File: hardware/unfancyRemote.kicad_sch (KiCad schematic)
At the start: 42 parts, among them J3 HALL1/PPM, J4 HALL2, J6 VIN, J7 VBAT, J8 Motor, Q1 AO3401A, Q2 MMBT3904, Q3 MMBT3904, SW1 SW_Push, U1 E28-2G4M12S, U2 MCP73871-2AA, U3 ESP32-C3_SUPERMINI

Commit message: wip
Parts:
- U3: footprint ESP32-C3_SUPERMINI:MODULE_ESP32-C3_SUPERMINI -> unfancyRemote_components:MODULE_ESP32-C3_SUPERMINI; symbol ESP32-C3_SUPERMINI:ESP32-C3_SUPERMINI -> unfancyRemote_components:ESP32-C3_SUPERMINI
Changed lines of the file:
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@@
 	)
 	(symbol
-		(lib_id "ESP32-C3_SUPERMINI:ESP32-C3_SUPERMINI")
+		(lib_id "unfancyRemote_components:ESP32-C3_SUPERMINI")
 		(at 135.89 36.83 0)
 		(unit 1)
@@
 			)
 		)
-		(property "Footprint" "ESP32-C3_SUPERMINI:MODULE_ESP32-C3_SUPERMINI"
+		(property "Footprint" "unfancyRemote_components:MODULE_ESP32-C3_SUPERMINI"
 			(at 135.89 36.83 0)
 			(effects

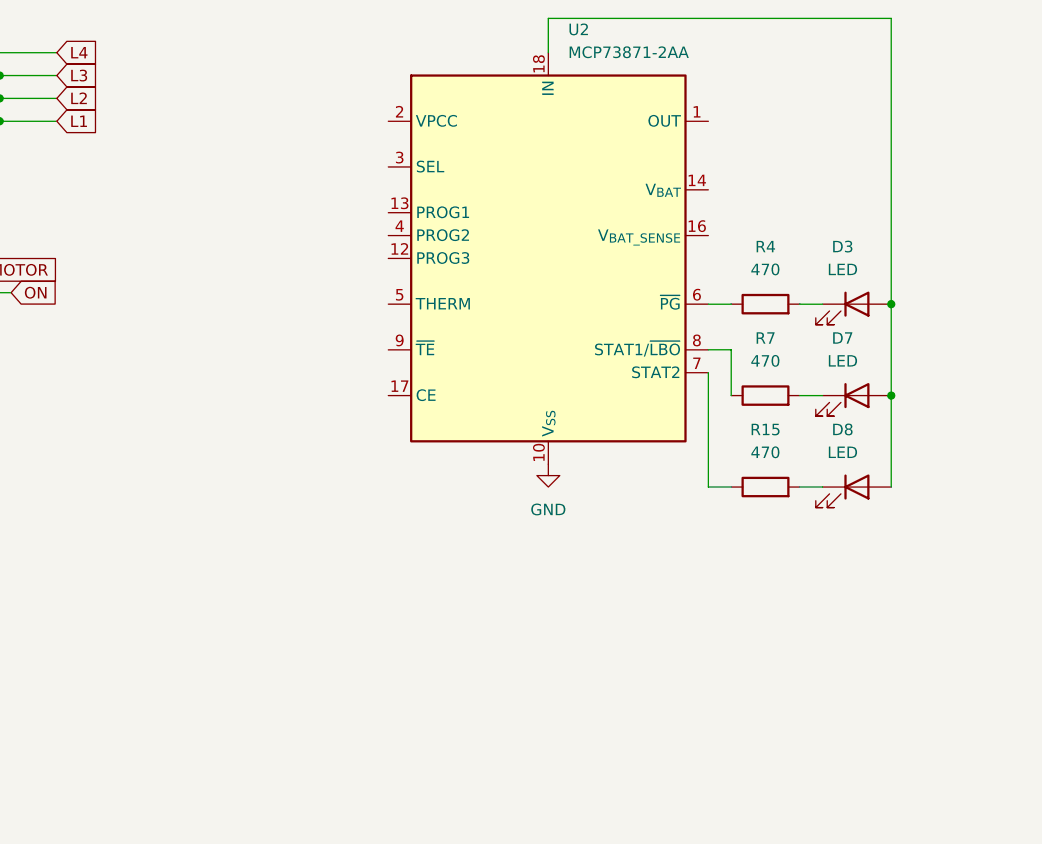
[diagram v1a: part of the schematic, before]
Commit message: finished charging ic wiring
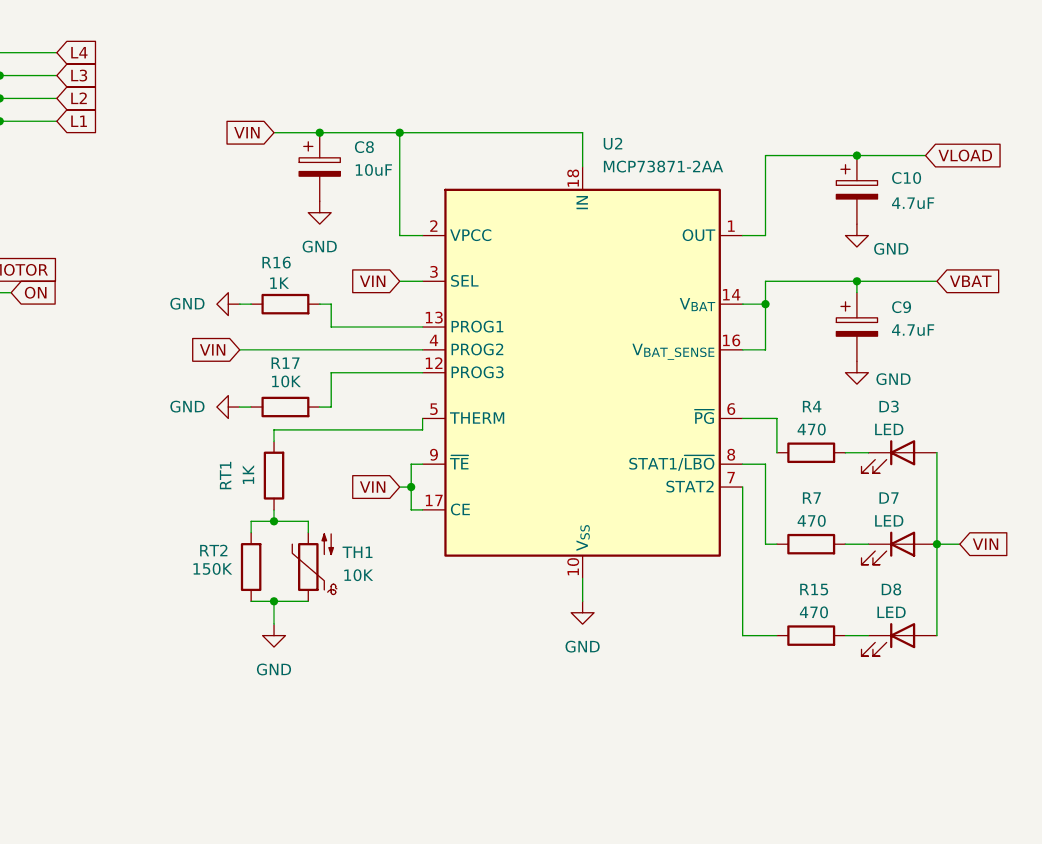
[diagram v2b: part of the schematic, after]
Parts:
- added C10, C9: 4.7uF, symbol Device:C_Polarized
- added C8: 10uF, symbol Device:C_Polarized
- added R16, RT1: 1K, Resistor_SMD:R_0603_1608Metric, symbol Device:R
- added R17: 10K, Resistor_SMD:R_0603_1608Metric, symbol Device:R
- added RT2: 150K, Resistor_SMD:R_0603_1608Metric, symbol Device:R
- added TH1: 10K, symbol Device:Thermistor_NTC
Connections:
- net GND: now also C10.2, C8.2, C9.2, R16.1, R17.1, RT2.1, TH1.1
- net VIN: now reaches D3.2 (A), D7.2 (A), D8.2 (A), U2.18 (IN), U2.19 (IN)
- net VIN: now also U2.17 (CE), U2.2 (VPCC), U2.3 (SEL), U2.4 (PROG2), U2.9 (~{TE}), C8.1
- net VLOAD: now reaches U2.1 (OUT), U2.20 (OUT)
- net VLOAD: now also C10.1
- net at U2.12 (PROG3): now also R17.2
- net at U2.13 (PROG1): now also R16.2
- net VBAT: now reaches U2.14 (V_{BAT}), U2.15 (V_{BAT})
- net VBAT: now also U2.16 (V_{BAT_SENSE}), C9.1
- net at U2.5 (THERM): now also RT1.2
- new net: RT1.1, RT2.2, TH1.2
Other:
- moved on the sheet: D3, D7, D8, R15, R4, R7, U2

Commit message: power progress
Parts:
- removed C1, C2, C3, C4, C5, C6: 1uF, Capacitor_SMD:C_0603_1608Metric, symbol Device:C
- removed D4, D5, D6: LED, LED_SMD:LED_0805_2012Metric, symbol Device:LED
- removed J7: VBAT, Connector_wire:SolderWirePad_1x01_SMD_1x2mm, symbol Connector_Generic:Conn_01x01
- removed R10, R8, R9: 220, Resistor_SMD:R_0603_1608Metric, symbol Device:R
- added C11, C13, C14, C6: 10uF, Capacitor_Tantalum_SMD:CP_EIA-3216-10_Kemet-I, symbol Device:C_Polarized
- added C12, C15: 1uF, Capacitor_SMD:C_0402_1005Metric, symbol Device:C
- added C16: 100nF, Capacitor_SMD:C_0402_1005Metric, symbol Device:C
- added D10, D4, D5, D6: WS2812B, LED_SMD:LED_WS2812B-2020_PLCC4_2.0x2.0mm, symbol LED:WS2812B-2020
- added D9: D_Schottky, Diode_SMD:D_SOD-523, symbol Device:D_Schottky
- added J1: Battery, unfancyRemote_components:SolderWirePad_1x02_SMD_1x2mm, symbol Connector_Generic:Conn_01x02
- added L1: 3.3uH, Inductor_SMD:L_01005_0402Metric, symbol Device:L
- added R18: 18.2K, Resistor_SMD:R_0402_1005Metric, symbol Device:R
- added R19: 68K, Resistor_SMD:R_0402_1005Metric, symbol Device:R
- added R20: 27K, Resistor_SMD:R_0402_1005Metric, symbol Device:R
- added U4: TPS61085DGK, Package_SO:VSSOP-8_3x3mm_P0.65mm, symbol Regulator_Switching:TPS61085DGK
- added U5: MIC5219-3.3YM5, Package_TO_SOT_SMD:SOT-23-5, symbol Regulator_Linear:MIC5219-3.3YM5
- C10, C8, C9: footprint (none) -> Capacitor_Tantalum_SMD:CP_EIA-3216-10_Kemet-I
- C7: value 1uF -> 1.6nF; footprint Capacitor_SMD:C_0603_1608Metric -> Capacitor_SMD:C_0402_1005Metric
- R1, R11, R12, R13, R14, R15, R16, R17, R2, R3, R4, R5, R6, R7, RT1, RT2: footprint Resistor_SMD:R_0603_1608Metric -> Resistor_SMD:R_0402_1005Metric
- TH1: footprint (none) -> Resistor_SMD:R_0402_1005Metric
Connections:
- net +3V3: now also C14.1, C15.1, C16.1, U5.5 (OUT)
- net +5V: now also C13.1, D10.4 (VDD), D4.4 (VDD), D5.4 (VDD), D6.4 (VDD), U5.1 (IN), U5.3 (EN); no longer U3.5V
- net 5VRAW: now also C6.1, D9.1 (K), R19.2; no longer C7.1
- net GND: now also C11.2, C12.1, C13.2, C14.2, C15.2, C16.2, C6.2, D10.2 (VSS), D4.2 (VSS), D5.2 (VSS), D6.2 (VSS), J1.2 (Pin_2), R18.1, U4.4 (GND), U5.2 (GND)
- net VBAT: now also R12.1, J1.1 (Pin_1)
- net VIN: now also U3.5V
- net VLOAD: now also C11.1, C12.2, L1.1, U4.3 (EN), U4.6 (VIN), U4.7 (FREQ)
- net L1 renamed LED
- net LED: now also D4.3 (DIN)
- new net: R18.2, R19.1, U4.2 (FB)
- new net: C7.1, R20.1
- new net: D9.2 (A), L1.2, U4.5 (SW)
- new net: D10.3 (DIN), D6.1 (DOUT)
- new net: D4.1 (DOUT), D5.3 (DIN)
- new net: D5.1 (DOUT), D6.3 (DIN)
- new net: R20.2, U4.1 (COMP)
- no-connect marks 3 -> 6
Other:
- moved on the sheet: R12, R13

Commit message: routing
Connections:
- net HALL1 is gone; now on net HALL1/PPM: U3.0 (GPIO0)
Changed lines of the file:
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@@
-	)
-	(junction
-		(at 104.14 25.4)
-		(diameter 0)
-		(color 0 0 0 0)
 	)
 	(junction
@@
 	(wire
 		(pts
-			(xy 101.6 22.86) (xy 104.14 22.86)
-		)
-		(stroke
-			(width 0)
-			(type default)
-		)
-	)
-	(wire
-		(pts
 			(xy 110.49 41.91) (xy 118.11 41.91)
 		)
@@
 	(wire
 		(pts
-			(xy 106.68 25.4) (xy 104.14 25.4)
-		)
-		(stroke
-			(width 0)
-			(type default)
-		)
-	)
-	(wire
-		(pts
 			(xy 81.28 59.69) (xy 87.63 59.69)
 		)
@@
 	(wire
 		(pts
-			(xy 104.14 22.86) (xy 104.14 25.4)
-		)
-		(stroke
-			(width 0)
-			(type default)
-		)
-	)
-	(wire
-		(pts
 			(xy 176.53 25.4) (xy 170.18 25.4)
 		)
@@
 	(wire
 		(pts
-			(xy 101.6 25.4) (xy 104.14 25.4)
+			(xy 101.6 25.4) (xy 106.68 25.4)
 		)
 		(stroke
@@
 		)
 	)
-	(global_label "PPM"
+	(global_label "HALL1{slash}PPM"
 		(shape input)
 		(at 101.6 25.4 180)
@@
 		)
 		(property "Intersheetrefs" "${INTERSHEET_REFS}"
-			(at 94.6234 25.4 0)
+			(at 87.6081 25.4 0)
 			(effects
 				(font
@@
 			(effects
 				(font
-					(size 1.27 1.27)
-				)
-				(justify right)
-				(hide yes)
-			)
-		)
-	)
-	(global_label "HALL1"
-		(shape input)
-		(at 101.6 22.86 180)
-		(fields_autoplaced yes)
-		(effects
-			(font
-				(size 1.27 1.27)
-			)
-			(justify right)
-		)
-		(property "Intersheetrefs" "${INTERSHEET_REFS}"
-			(at 92.93 22.86 0)
-			(effects
-				(font

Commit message: more routing
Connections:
- net +5V: now also J6.1 (Pin_1)
- net 5VRAW: no longer J6.1 (Pin_1)
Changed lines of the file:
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@@
 		)
 	)
-	(global_label "5VRAW"
+	(global_label "+5V"
 		(shape input)
 		(at 66.04 115.57 180)
@@
 		)
 		(property "Intersheetrefs" "${INTERSHEET_REFS}"
-			(at 57.5188 115.4906 0)
+			(at 59.1843 115.57 0)
 			(effects
 				(font
